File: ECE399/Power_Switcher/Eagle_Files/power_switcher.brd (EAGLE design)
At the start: 132 x 132 mm, 69 parts, among them J1 BANNANA_DEV, J2 BANNANA_DEV, J3 BANNANA_DEV, J4 BANNANA_DEV, J5 BANNANA_DEV, J6 BANNANA_DEV, J7 BANNANA_DEV, Q1 TRANSISTOR_DEV, Q2 TRANSISTOR_DEV, Q3 TRANSISTOR_DEV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

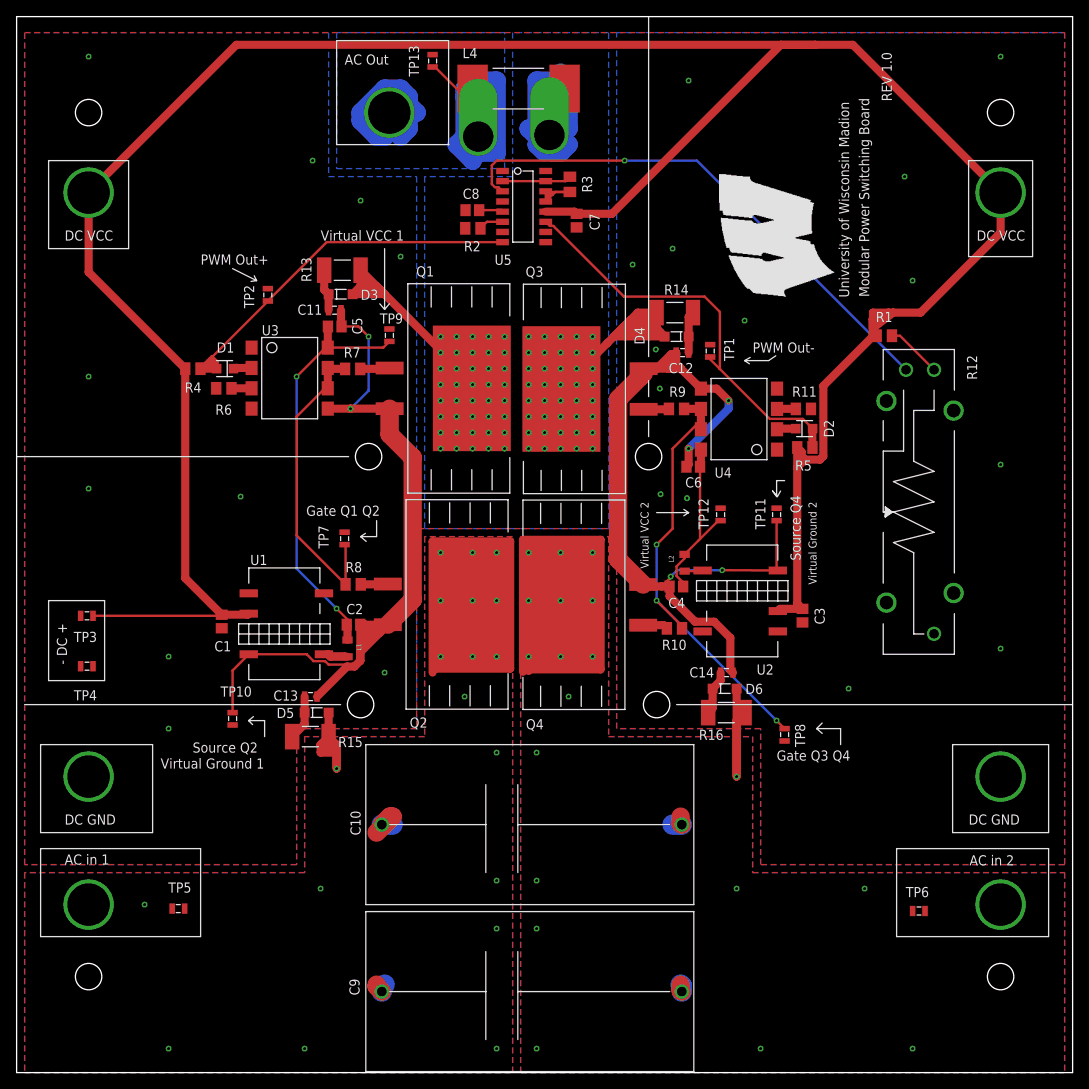
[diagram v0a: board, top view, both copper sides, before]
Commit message: diodes moved for Giri
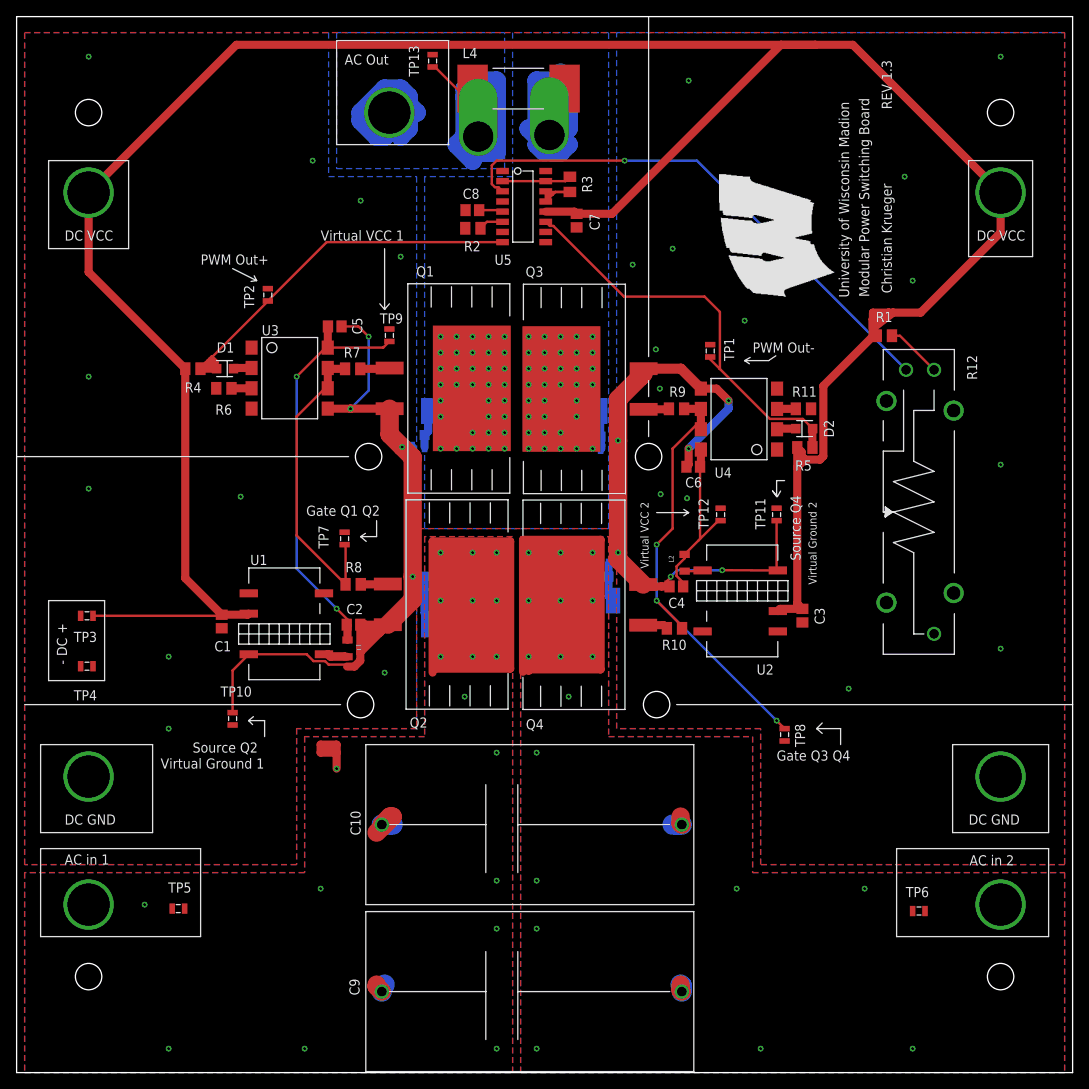
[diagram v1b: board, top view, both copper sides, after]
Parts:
- moved R16 25.2 mm to (69.0, 58.0), flipped to the bottom
- moved D6 23.6 mm to (70.0, 61.0), flipped to the bottom
- moved D5 22.7 mm to (53.0, 61.0), flipped to the bottom, turned to 0 degrees
- moved R15 22.0 mm to (55.0, 55.0), flipped to the bottom, turned to 0 degrees
- moved R13 21.9 mm to (55.0, 81.7), flipped to the bottom, turned to 0 degrees
- moved D3 21.3 mm to (53.0, 78.7), flipped to the bottom, turned to 0 degrees
- moved C11 20.9 mm to (50.0, 77.2), flipped to the bottom
- moved C13 20.1 mm to (50.0, 59.4), flipped to the bottom
- moved C14 19.5 mm to (73.0, 62.6), flipped to the bottom, turned to 180 degrees
- moved R14 16.9 mm to (67.4, 81.7), flipped to the bottom, turned to 180 degrees
- moved D4 16.7 mm to (69.0, 78.5), flipped to the bottom, turned to 180 degrees
- moved C12 16.3 mm to (72.0, 77.0), flipped to the bottom
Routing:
- net N$28: track 113.2 -> 43.6 mm, vias 80 -> 68
- net N$3: track 100.1 -> 79.6 mm, vias 4 -> 6
- net AC_IN_2: track 75.1 -> 59.1 mm, vias 19 -> 18
- net N$14: track 108.9 -> 99.8 mm, vias 2 -> 4
- net AC_IN_1: track 76.7 -> 67.9 mm
- net N$36: track 5.64 -> 4.83 mm
- net N$33: track 5.64 -> 6.19 mm
- net N$27: track 5.23 -> 4.69 mm
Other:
- board text added: "Christian Krueger"
- board text added: "REV 1.3"
- board text removed: "REV 1.0"

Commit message: right diode added
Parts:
- D3, D4, D5, D6: value SOD_DIODE_DEV -> D2PAK_DIODE_DEV; device power_switcher:SOD_DIODE_PKG -> blizzard_common_1:D2PAK_PKG
- moved R14 13.3 mm to (70.4, 94.7)
- moved R13 12.4 mm to (52.0, 93.7)
- moved R15 10.9 mm to (51.5, 44.7)
- moved R16 10.2 mm to (71.0, 48.0)
- moved D4 10.0 mm to (75.0, 86.5), turned to 90 degrees
- moved D5 10.0 mm to (47.0, 53.0), turned to 270 degrees
- moved D3 8.04 mm to (48.0, 85.0), turned to 270 degrees
- moved D6 6.44 mm to (74.4, 56.3), turned to 90 degrees
- moved L3 3.00 mm to (60.8, 62.3)
- moved C12 2.33 mm to (72.4, 79.3)
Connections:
- removed net N$28: D3.P$1, D4.P$1, L3.P$2, L4.P$2, Q1.D, Q3.D, R13.P$1, R14.P$1
- new net PRE_AC_OUT: D3.IN1, D3.IN2, D4.IN1, D4.IN2, L3.P$2, L4.P$2, Q1.D, Q3.D, R13.P$1, R14.P$1
- net AC_IN_1: now also D5.IN1, D5.IN2; no longer D5.P$1
- net AC_IN_2: now also D6.IN1, D6.IN2; no longer D6.P$1
- net N$27: now also D3.OUT; no longer D3.P$2
- net N$30: now also D4.OUT; no longer D4.P$2
- net N$33: now also D5.OUT; no longer D5.P$2
- net N$36: now also D6.OUT; no longer D6.P$2
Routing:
- net PRE_AC_OUT: track 0.00 -> 54.3 mm, vias 0 -> 70
- net N$28: track 43.6 -> 0.00 mm, vias 68 -> 0
- net N$27: track 4.69 -> 17.6 mm
- net N$36: track 4.83 -> 17.2 mm
- net N$30: track 4.76 -> 16.8 mm
- net N$33: track 6.19 -> 16.0 mm
- net DC_VCC_RAW: track 334.4 -> 329.7 mm
- net AC_IN_2: track 59.1 -> 55.7 mm, vias 18 -> 28
- net N$14: track 99.8 -> 96.8 mm
- net N$22: track 57.1 -> 55.4 mm
- net AC_OUT: track 96.8 -> 97.6 mm, vias 0 -> 4
- net AC_IN_1: vias 19 -> 29
- added copper zone on layer 16, net PRE_AC_OUT
- removed copper zone on layer 16, net N$28
